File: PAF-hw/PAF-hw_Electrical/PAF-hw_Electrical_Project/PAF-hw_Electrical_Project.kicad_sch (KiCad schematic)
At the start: 7 parts, among them J5 Barrel_Jack_Switch, U1 ESP32-S3-WROOM-1

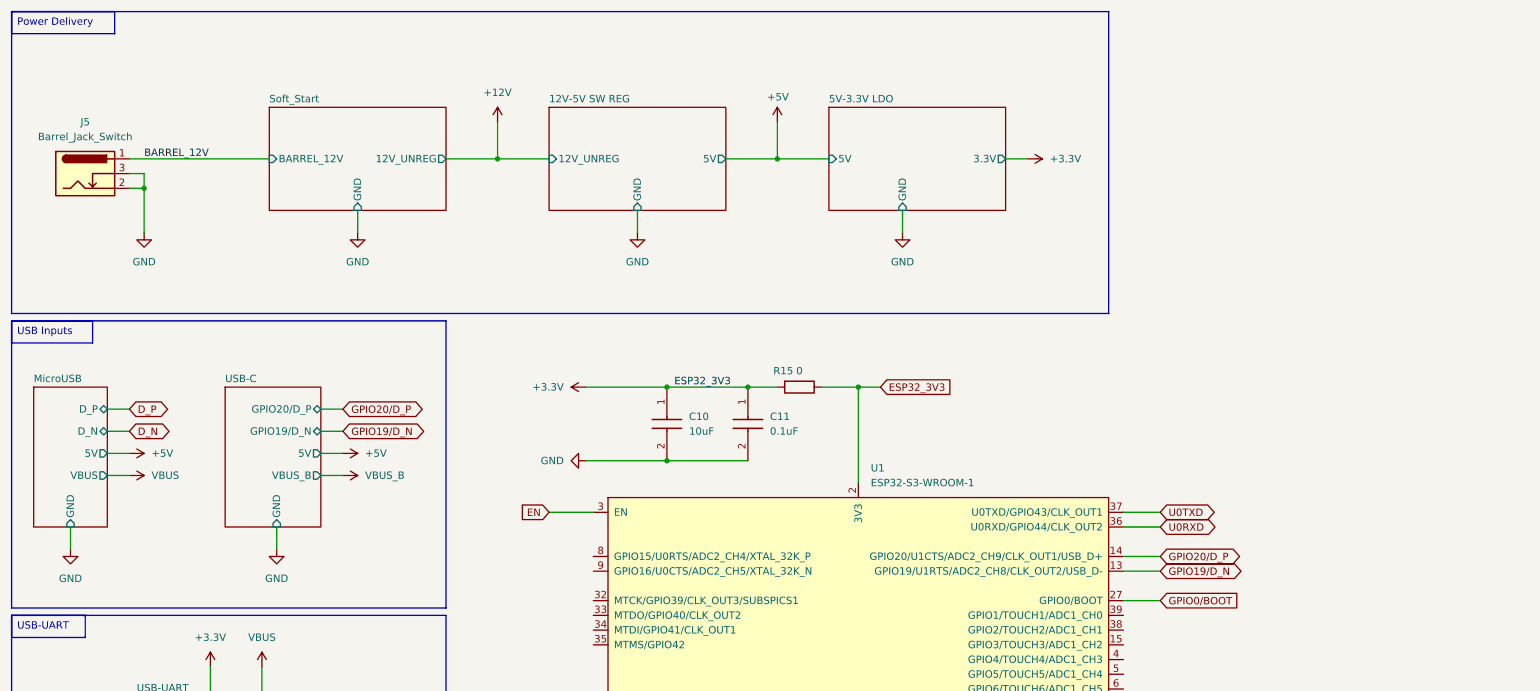
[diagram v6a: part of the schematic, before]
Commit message: Added motor driver to schematic.
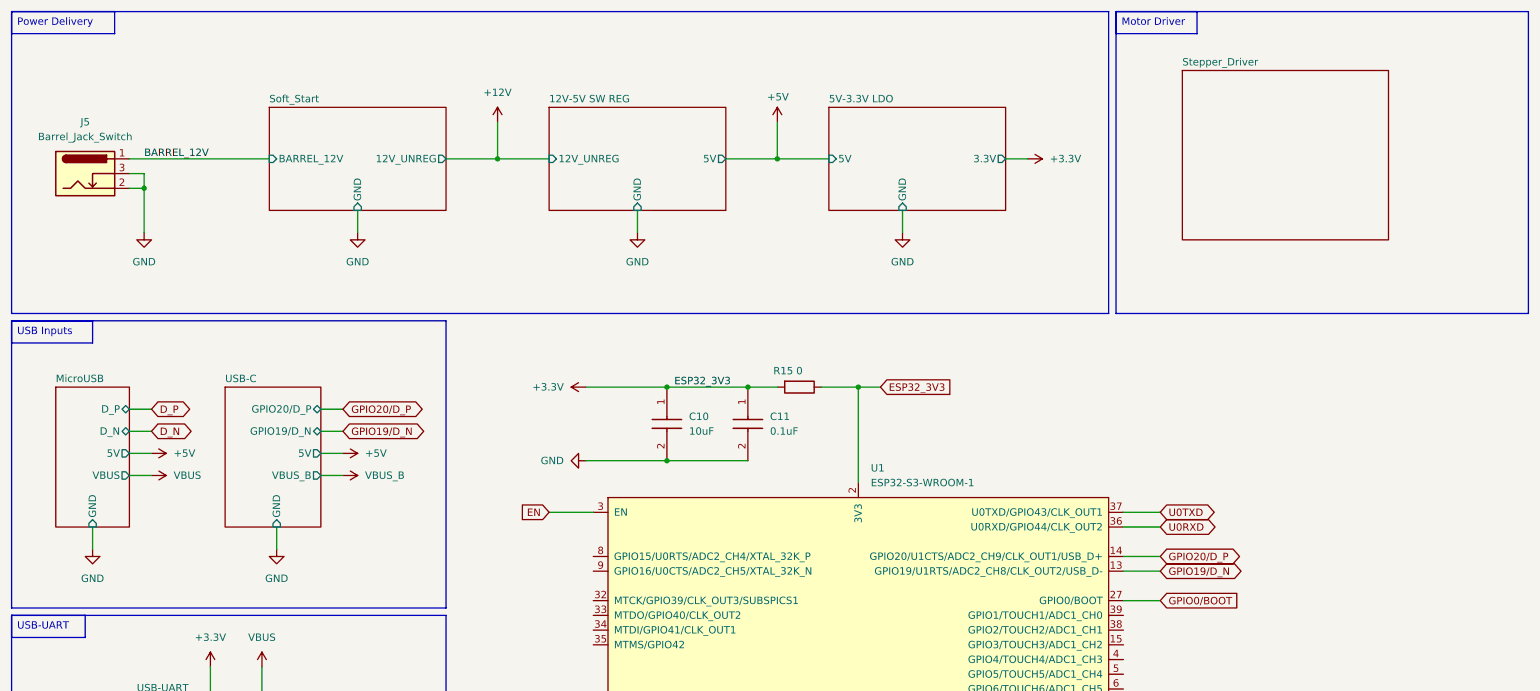
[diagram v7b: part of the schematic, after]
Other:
- added sheet Stepper_Driver (Stepper_Driver.kicad_sch)
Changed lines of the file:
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@@
 	)
 	(rectangle
+		(start 204.47 13.97)
+		(end 275.59 66.04)
+		(stroke
+			(width 0)
+			(type default)
+		)
+		(fill
+			(type none)
+		)
+	)
+	(rectangle
 		(start 13.97 13.97)
 		(end 203.2 66.04)
@@
 		)
 	)
+	(text_box "Motor Driver\n"
+		(exclude_from_sim no)
+		(at 204.47 13.97 0)
+		(size 13.97 3.81)
+		(margins 0.9525 0.9525 0.9525 0.9525)
+		(stroke
+			(width 0)
+			(type solid)
+		)
+		(fill
+			(type none)
+		)
+		(effects
+			(font
+				(size 1.27 1.27)
+			)
+			(justify left top)
+		)
+	)
 	(text_box "Reset and Boot Switches\n"
 		(exclude_from_sim no)
@@
 	(wire
 		(pts
-			(xy 30.48 82.55) (xy 34.29 82.55)
+			(xy 34.29 82.55) (xy 38.1 82.55)
 		)
 		(stroke
@@
 	(wire
 		(pts
-			(xy 30.48 90.17) (xy 34.29 90.17)
+			(xy 34.29 90.17) (xy 38.1 90.17)
 		)
 		(stroke
@@
 	(wire
 		(pts
-			(xy 24.13 102.87) (xy 24.13 106.68)
+			(xy 27.94 102.87) (xy 27.94 106.68)
 		)
 		(stroke
@@
 	(wire
 		(pts
-			(xy 30.48 86.36) (xy 34.29 86.36)
+			(xy 34.29 86.36) (xy 38.1 86.36)
 		)
 		(stroke
@@
 	(wire
 		(pts
-			(xy 30.48 93.98) (xy 34.29 93.98)
+			(xy 34.29 93.98) (xy 38.1 93.98)
 		)
 		(stroke
@@
 	(global_label "D_P"
 		(shape bidirectional)
-		(at 34.29 82.55 0)
+		(at 38.1 82.55 0)
 		(fields_autoplaced yes)
 		(effects
@@
 		)
 		(property "Intersheetrefs" "${INTERSHEET_REFS}"
-			(at 41.8941 82.55 0)
+			(at 45.7041 82.55 0)
 			(effects
 				(font
@@
 	(global_label "D_N"
 		(shape bidirectional)
-		(at 34.29 86.36 0)
+		(at 38.1 86.36 0)
 		(fields_autoplaced yes)
 		(effects
@@
 		)
 		(property "Intersheetrefs" "${INTERSHEET_REFS}"
-			(at 41.9546 86.36 0)
+			(at 45.7646 86.36 0)
 			(effects
 				(font
@@
 	(symbol
 		(lib_id "power:+5V")
-		(at 34.29 90.17 270)
+		(at 38.1 90.17 270)
 		(unit 1)
 		(exclude_from_sim no)
@@
 		(dnp no)
 		(property "Reference" "#PWR041"
-			(at 30.48 90.17 0)
+			(at 34.29 90.17 0)
 			(effects
 				(font
@@
 		)
 		(property "Value" "+5V"
-			(at 38.1 90.1699 90)
+			(at 41.91 90.1699 90)
 			(effects
 				(font
@@
 		)
 		(property "Footprint" ""
-			(at 34.29 90.17 0)
+			(at 38.1 90.17 0)
 			(effects
 				(font
@@
 		)
 		(property "Datasheet" ""
-			(at 34.29 90.17 0)
+			(at 38.1 90.17 0)
 			(effects
 				(font
@@
 		)
 		(property "Description" "Power symbol creates a global label with name \"+5V\""
-			(at 34.29 90.17 0)
+			(at 38.1 90.17 0)
 			(effects
 				(font
@@
 	(symbol
 		(lib_id "power:VBUS")
-		(at 34.29 93.98 270)
+		(at 38.1 93.98 270)
 		(unit 1)
 		(exclude_from_sim no)
@@
 		(fields_autoplaced yes)
 		(property "Reference" "#PWR042"
-			(at 30.48 93.98 0)
+			(at 34.29 93.98 0)
 			(effects
 				(font
@@
 		)
 		(property "Value" "VBUS"
-			(at 38.1 93.9799 90)
+			(at 41.91 93.9799 90)
 			(effects
 				(font
@@
 		)
 		(property "Footprint" ""
-			(at 34.29 93.98 0)
+			(at 38.1 93.98 0)
 			(effects
 				(font
@@
 		)
 		(property "Datasheet" ""
-			(at 34.29 93.98 0)
+			(at 38.1 93.98 0)
 			(effects
 				(font
@@
 		)
 		(property "Description" "Power symbol creates a global label with name \"VBUS\""
-			(at 34.29 93.98 0)
+			(at 38.1 93.98 0)
 			(effects
 				(font
@@
 	(symbol
 		(lib_id "power:GND")
-		(at 24.13 106.68 0)
+		(at 27.94 106.68 0)
 		(unit 1)
 		(exclude_from_sim no)
@@
 		(fields_autoplaced yes)
 		(property "Reference" "#PWR033"
-			(at 24.13 113.03 0)
+			(at 27.94 113.03 0)
 			(effects
 				(font
@@
 		)
 		(property "Value" "GND"
-			(at 24.13 111.76 0)
+			(at 27.94 111.76 0)
 			(effects
 				(font
@@
 		)
 		(property "Footprint" ""
-			(at 24.13 106.68 0)
+			(at 27.94 106.68 0)
 			(effects
 				(font
@@
 		)
 		(property "Datasheet" ""
-			(at 24.13 106.68 0)
+			(at 27.94 106.68 0)
 			(effects
 				(font
@@
 		)
 		(property "Description" "Power symbol creates a global label with name \"GND\" , ground"
-			(at 24.13 106.68 0)
+			(at 27.94 106.68 0)
 			(effects
 				(font
@@
 	)
 	(sheet
-		(at 17.78 78.74)
+		(at 21.59 78.74)
 		(size 12.7 24.13)
 		(exclude_from_sim no)
@@
 		)
 		(property "Sheetname" "MicroUSB"
-			(at 17.78 78.0284 0)
+			(at 21.59 78.0284 0)
 			(effects
 				(font
@@
 		)
 		(property "Sheetfile" "MicroUSB.kicad_sch"
-			(at 17.78 103.4546 0)
+			(at 21.59 103.4546 0)
 			(effects
 				(font
@@
 		)
 		(pin "D_P" bidirectional
-			(at 30.48 82.55 0)
+			(at 34.29 82.55 0)
 			(effects
 				(font
@@
 		)
 		(pin "D_N" bidirectional
-			(at 30.48 86.36 0)
+			(at 34.29 86.36 0)
 			(effects
 				(font
@@
 		)
 		(pin "5V" output
-			(at 30.48 90.17 0)
+			(at 34.29 90.17 0)
 			(effects
 				(font
@@
 		)
 		(pin "VBUS" output
-			(at 30.48 93.98 0)
+			(at 34.29 93.98 0)
 			(effects
 				(font
@@
 		)
 		(pin "GND" input
-			(at 24.13 102.87 270)
+			(at 27.94 102.87 270)
 			(effects
 				(font
@@
 				)
 			)
+		)
+	)
+	(sheet
+		(at 215.9 24.13)
+		(size 35.56 29.21)
+		(exclude_from_sim no)
+		(in_bom yes)
+		(on_board yes)
+		(dnp no)
+		(fields_autoplaced yes)
+		(stroke
+			(width 0.1524)
+			(type solid)
+		)
+		(fill
+			(color 0 0 0 0.0000)
+		)
+		(property "Sheetname" "Stepper_Driver"
+			(at 215.9 23.4184 0)
+			(effects
+				(font
+					(size 1.27 1.27)
+				)
+				(justify left bottom)
+			)
+		)
+		(property "Sheetfile" "Stepper_Driver.kicad_sch"
+			(at 215.9 53.9246 0)
+			(effects
+				(font
+					(size 1.27 1.27)
+				)
+				(justify left top)
+				(hide yes)
+			)
+		)
+		(instances
+			(project "PAF-hw_Electrical_Project"
+				(path "/c6f2fd82-4900-4fc0-ba31-c37e114de4ed"
+					(page "10")
+				)
+			)

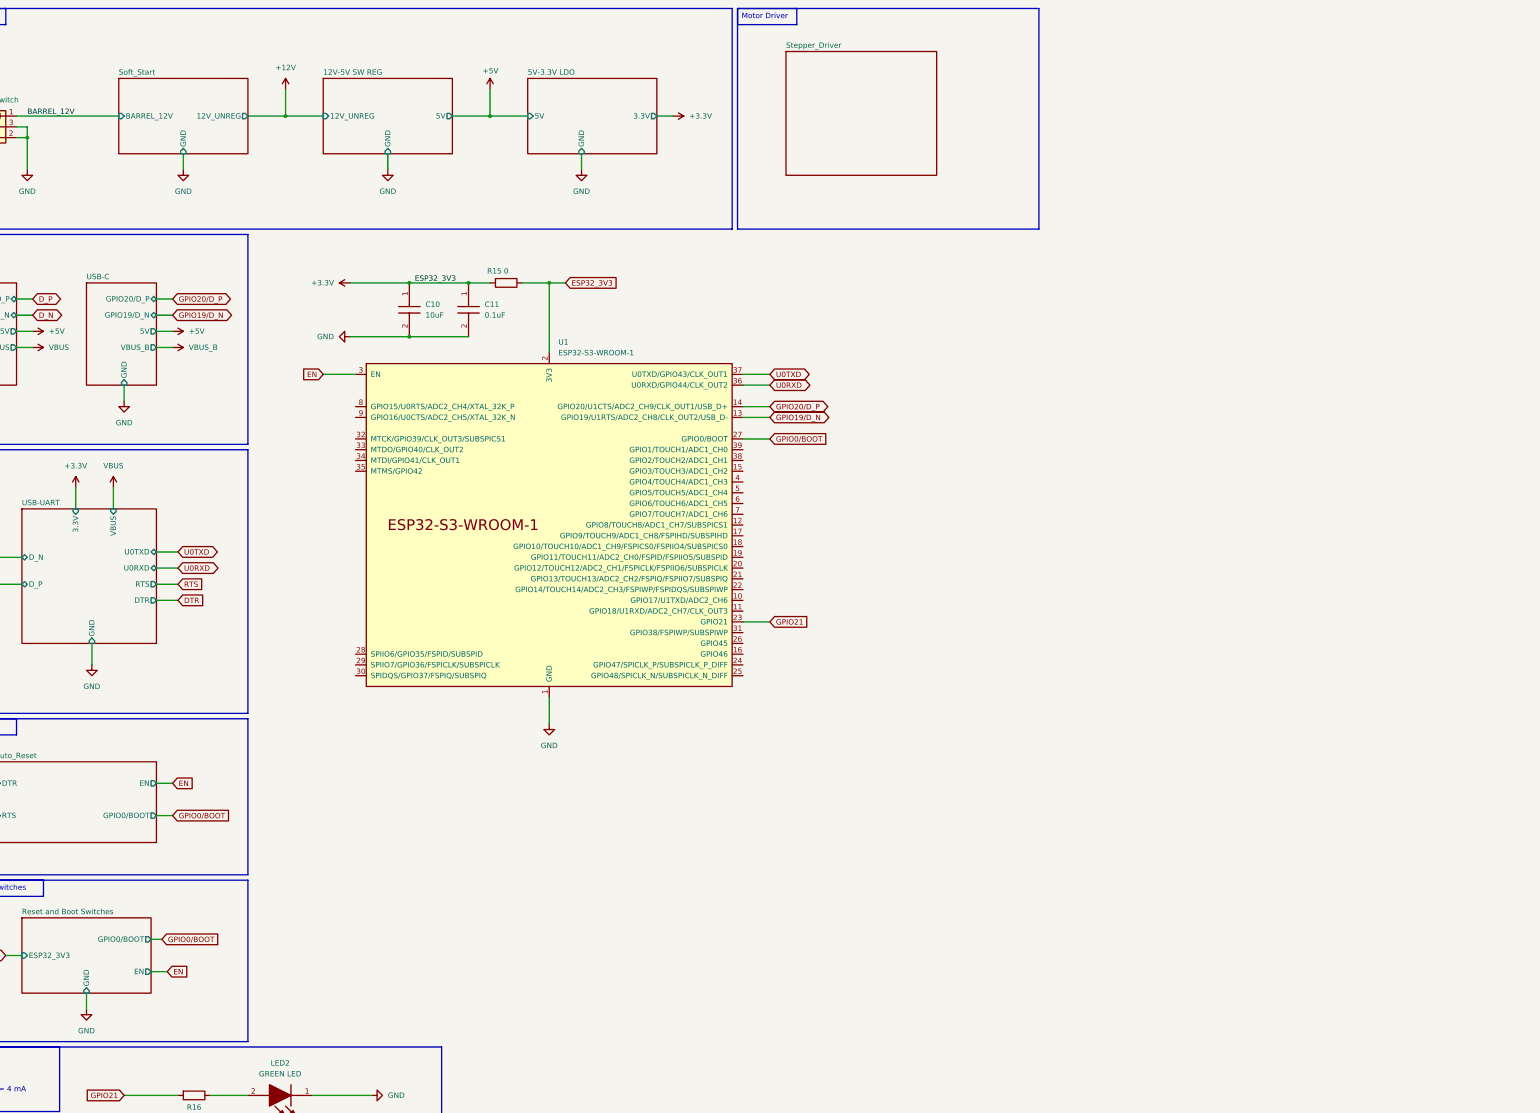
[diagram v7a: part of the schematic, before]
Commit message: Added camera circuit to schematic.
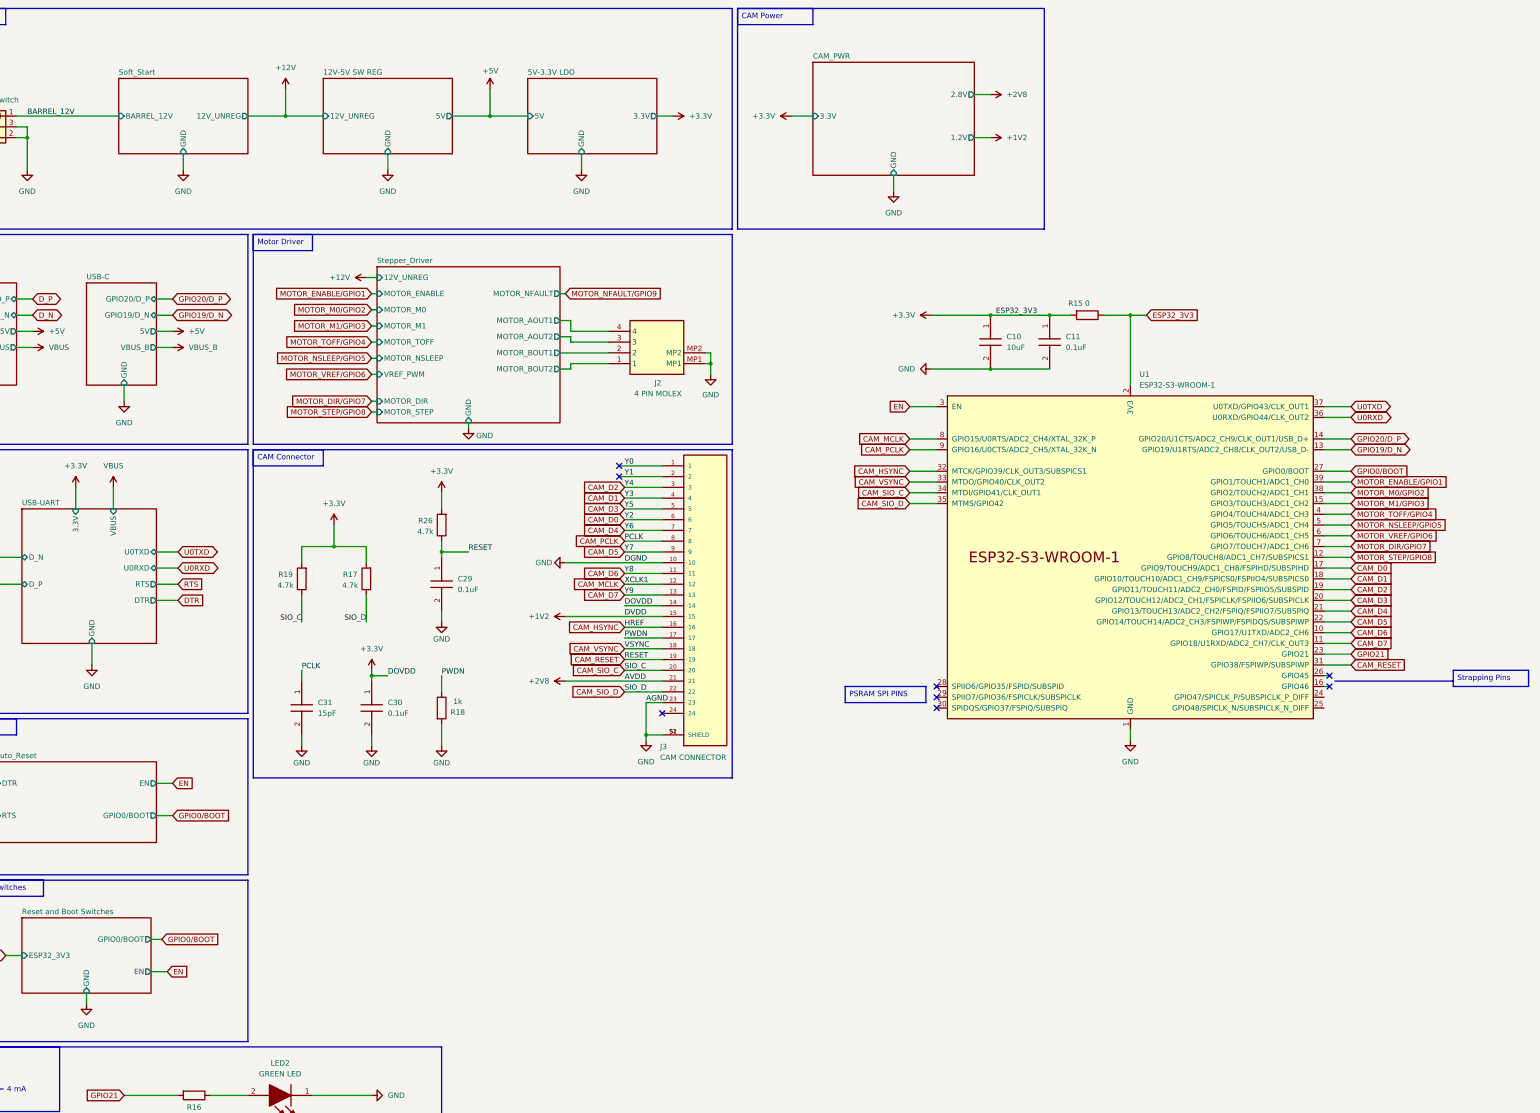
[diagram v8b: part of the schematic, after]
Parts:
- added C29, C30: 0.1uF, C0603, symbol SamacSys_Parts:C0603C104K5RACTU
- added C31: 15pF, C0402, symbol SamacSys_Parts:C0402C150J8HACTU
- added J2: 4 PIN MOLEX, 5025850470, symbol SamacSys_Parts:502585-0470
- added J3: CAM CONNECTOR, FFC2B28-24-G:GCT_FFC2B28-24-G, symbol FFC2B28-24-G:FFC2B28-24-G
- added R17, R19, R26: 4.7k, symbol Device:R
- added R18: 1k, symbol Device:R
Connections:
- net +3.3V: now also C30.1, J3.14, R17.2, R19.2, R26.2
- net GND: now also C29.2, C30.2, C31.2, J2.MP1, J2.MP2, J3.10, J3.23, J3.S1 (SHIELD), J3.S2 (SHIELD), R18.2
- net CAM_D6: now reaches U1.10 (GPIO17/U1TXD/ADC2_CH6)
- net CAM_D6: now also J3.11
- net CAM_D7: now reaches U1.11 (GPIO18/U1RXD/ADC2_CH7/CLK_OUT3)
- net CAM_D7: now also J3.13
- net MOTOR_STEP/GPIO8: now reaches U1.12 (GPIO8/TOUCH8/ADC1_CH7/SUBSPICS1)
- net MOTOR_M1/GPIO3: now reaches U1.15 (GPIO3/TOUCH3/ADC1_CH2)
- net CAM_D0: now reaches U1.17 (GPIO9/TOUCH9/ADC1_CH8/FSPIHD/SUBSPIHD)
- net CAM_D0: now also J3.6
- net CAM_D1: now reaches U1.18 (GPIO10/TOUCH10/ADC1_CH9/FSPICS0/FSPIIO4/SUBSPICS0)
- net CAM_D1: now also J3.4
- net CAM_D2: now reaches U1.19 (GPIO11/TOUCH11/ADC2_CH0/FSPID/FSPIIO5/SUBSPID)
- net CAM_D2: now also J3.3
- net CAM_D3: now reaches U1.20 (GPIO12/TOUCH12/ADC2_CH1/FSPICLK/FSPIIO6/SUBSPICLK)
- net CAM_D3: now also J3.5
- net CAM_D4: now reaches U1.21 (GPIO13/TOUCH13/ADC2_CH2/FSPIQ/FSPIIO7/SUBSPIQ)
- net CAM_D4: now also J3.7
- net CAM_D5: now reaches U1.22 (GPIO14/TOUCH14/ADC2_CH3/FSPIWP/FSPIDQS/SUBSPIWP)
- net CAM_D5: now also J3.9
- net CAM_RESET: now reaches U1.31 (GPIO38/FSPIWP/SUBSPIWP)
- net CAM_RESET: now also C29.1, J3.19, R26.1
- net CAM_HSYNC: now reaches U1.32 (MTCK/GPIO39/CLK_OUT3/SUBSPICS1)
- net CAM_HSYNC: now also J3.16
- net CAM_VSYNC: now reaches U1.33 (MTDO/GPIO40/CLK_OUT2)
- net CAM_VSYNC: now also J3.18
- net CAM_SIO_C: now reaches U1.34 (MTDI/GPIO41/CLK_OUT1)
- net CAM_SIO_C: now also J3.20, R19.1
- net CAM_SIO_D: now reaches U1.35 (MTMS/GPIO42)
- net CAM_SIO_D: now also J3.22, R17.1
- net MOTOR_M0/GPIO2: now reaches U1.38 (GPIO2/TOUCH2/ADC1_CH1)
- net MOTOR_ENABLE/GPIO1: now reaches U1.39 (GPIO1/TOUCH1/ADC1_CH0)
- net MOTOR_TOFF/GPIO4: now reaches U1.4 (GPIO4/TOUCH4/ADC1_CH3)
- net MOTOR_NSLEEP/GPIO5: now reaches U1.5 (GPIO5/TOUCH5/ADC1_CH4)
- net MOTOR_VREF/GPIO6: now reaches U1.6 (GPIO6/TOUCH6/ADC1_CH5)
- net MOTOR_DIR/GPIO7: now reaches U1.7 (GPIO7/TOUCH7/ADC1_CH6)
- net CAM_MCLK: now reaches U1.8 (GPIO15/U0RTS/ADC2_CH4/XTAL_32K_P)
- net CAM_MCLK: now also J3.12
- net CAM_PCLK: now reaches U1.9 (GPIO16/U0CTS/ADC2_CH5/XTAL_32K_N)
- net CAM_PCLK: now also C31.1, J3.8
- new net +1V2: J3.15
- new net +2V8: J3.21
- new net PWDN: J3.17, R18.1
- new net Stepper_Driver/MOTOR_AOUT1: J2.4
- new net Stepper_Driver/MOTOR_AOUT2: J2.3
- new net Stepper_Driver/MOTOR_BOUT1: J2.2
- new net Stepper_Driver/MOTOR_BOUT2: J2.1
- new net Y0: J3.1
- new net Y1: J3.2
- no-connect marks 0 -> 8
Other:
- added sheet CAM_PWR (untitled.kicad_sch)
- sheet Stepper_Driver ports: added 12V_UNREG, GND, MOTOR_AOUT1, MOTOR_AOUT2, MOTOR_BOUT1, MOTOR_BOUT2, MOTOR_DIR, MOTOR_ENABLE, MOTOR_M0, MOTOR_M1, MOTOR_NFAULT, MOTOR_NSLEEP, MOTOR_STEP, MOTOR_TOFF, VREF_PWM; removed none
- moved on the sheet: C10, C11, R15, U1
